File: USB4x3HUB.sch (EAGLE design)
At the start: 106 parts, among them IC1 TUSB2036, IC10 SN74LVC1G139DCUR, IC2 FSUSB74MPX, IC6 3.3V, IC7 5V, IC8 5V, IC9 5V, Q1 CLOCK_OSC_4, SW1 RD, SW2 BL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

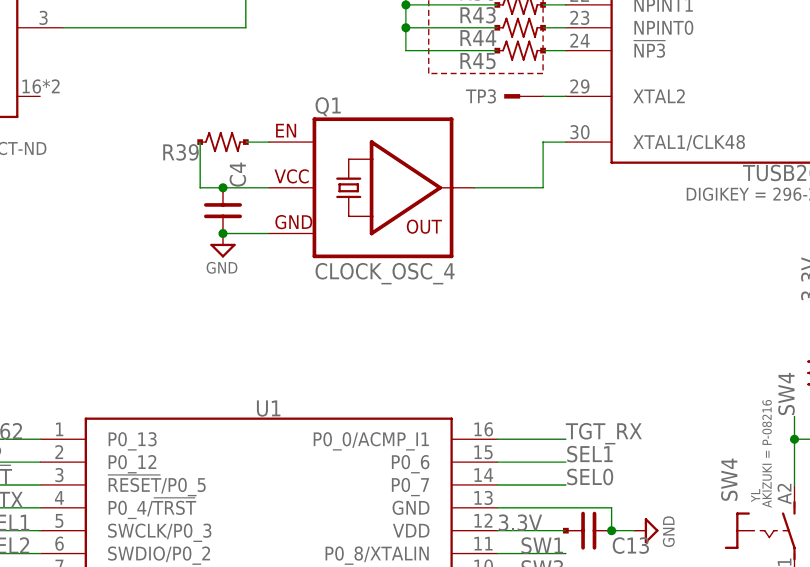
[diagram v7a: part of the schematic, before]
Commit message: library update; add DIGIKEY attributes
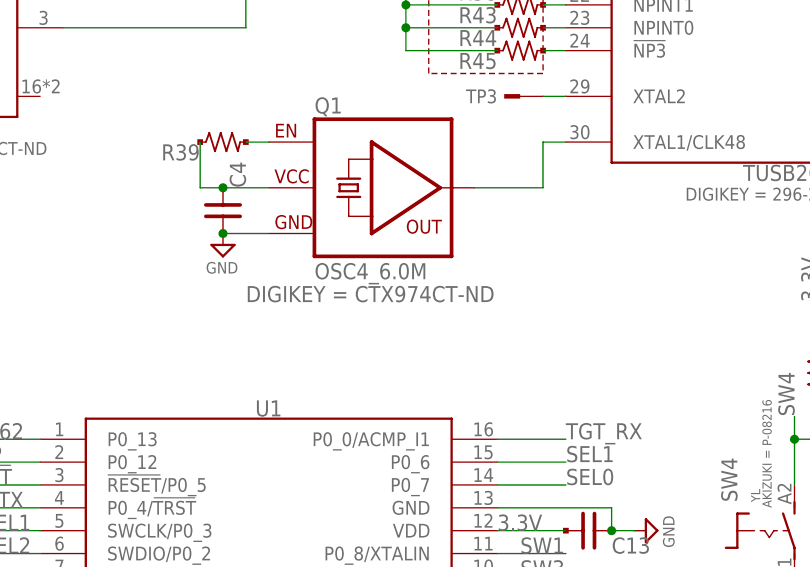
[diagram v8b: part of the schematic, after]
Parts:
- Q1: value CLOCK_OSC_4 -> OSC4_6.0M; device mylib:CLOCK_OSC_4 -> mylib:OSC4_6.0M
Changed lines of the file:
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@@
 <part name="R45" library="mylib" deviceset="R_US_*" device="_1005" technology="10K"/>
 <part name="R42" library="mylib" deviceset="R_US_*" device="_1005" technology="10K"/>
-<part name="Q1" library="mylib" deviceset="CLOCK_OSC_4" device=""/>
+<part name="Q1" library="mylib" deviceset="OSC4_*" device="" technology="6.0M" value="OSC4_6.0M"/>
 <part name="SUPPLY32" library="mylib" deviceset="GND" device=""/>
 <part name="TP3" library="mylib" deviceset="TESTPAD" device=""/>
@@
 <instance part="R45" gate="G$1" x="167.64" y="129.54"/>
 <instance part="R42" gate="G$1" x="101.6" y="71.12"/>
-<instance part="Q1" gate="G$1" x="152.4" y="114.3"/>
+<instance part="Q1" gate="G$1" x="152.4" y="114.3">
+<attribute name="DIGIKEY" x="137.16" y="101.6" size="1.778" layer="96" display="both"/>
+</instance>
 <instance part="SUPPLY32" gate="GND" x="134.62" y="106.68"/>
 <instance part="TP3" gate="1" x="167.64" y="124.46" rot="R180"/>
